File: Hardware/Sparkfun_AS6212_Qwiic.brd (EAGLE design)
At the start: 25.4 x 25.4 mm, 62 parts, among them J1 PTH, J2 QWIIC_RA, J3 QWIIC_RA, U2 AS6212

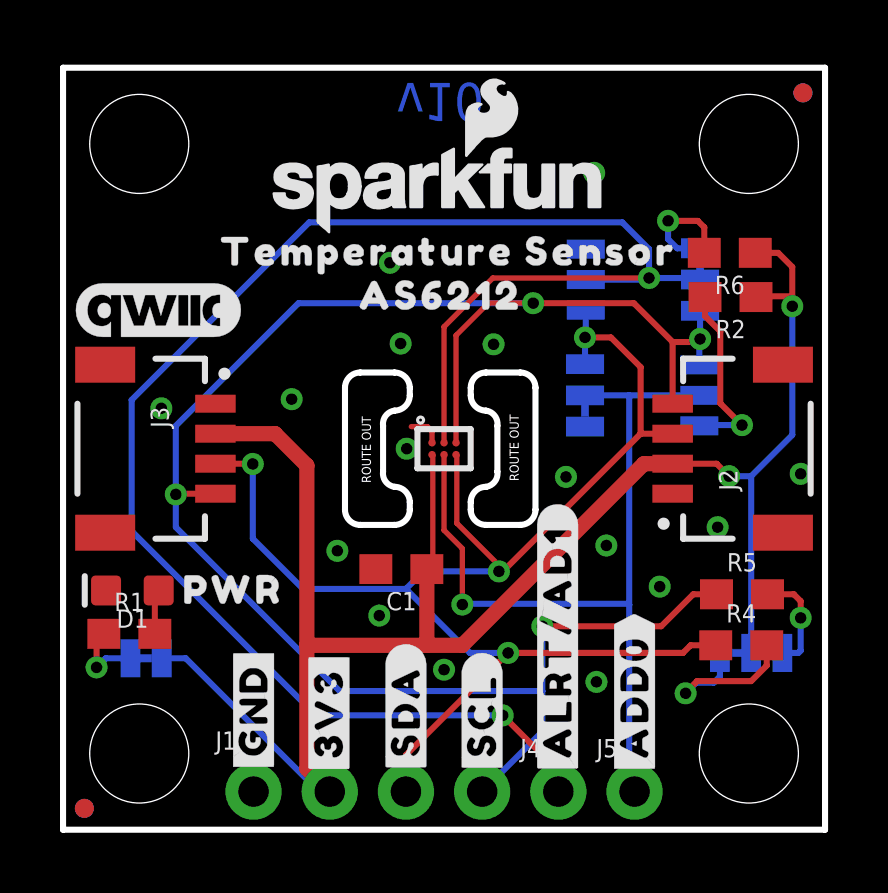
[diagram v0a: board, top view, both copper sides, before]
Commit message: nudged LED and I2C jumpers away from standoffs a tiny bit.
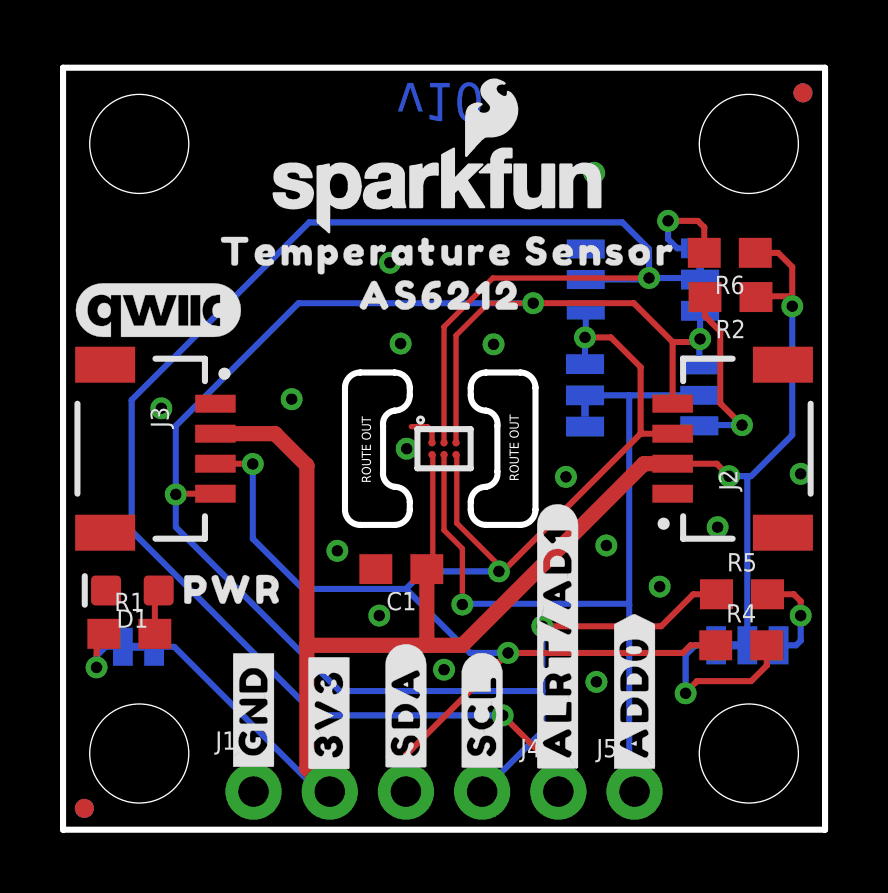
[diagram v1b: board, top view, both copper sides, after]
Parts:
- moved JP1 0.46 mm to (2.51, 6.10)
- moved U$18 0.38 mm to (21.2, 9.70)
- moved U$1 0.36 mm to (2.51, 7.70)
- moved I2C 0.28 mm to (22.8, 6.15)
- moved U$2 0.19 mm to (22.8, 7.75)
- moved U$8 0.13 mm to (21.2, 11.0)
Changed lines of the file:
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@@
 <setting verticaltext="up"/>
 </settings>
-<grid distance="0.05" unitdist="inch" unit="inch" style="lines" multiple="1" display="yes" altdistance="0.005" altunitdist="inch" altunit="inch"/>
+<grid distance="0.05" unitdist="inch" unit="inch" style="lines" multiple="1" display="yes" altdistance="0.001" altunitdist="inch" altunit="inch"/>
 <layers>
 <layer number="1" name="Top" color="4" fill="1" visible="yes" active="yes"/>
@@
 <element name="JP8" library="SparkFun-Hardware" package="STAND-OFF" value="STAND-OFF" x="22.86" y="22.86" smashed="yes"/>
 <element name="JP9" library="SparkFun-Hardware" package="STAND-OFF" value="STAND-OFF" x="2.54" y="22.86" smashed="yes"/>
-<element name="I2C" library="SparkFun-Jumpers" package="SMT-JUMPER_3_2-NC_TRACE_SILK" package3d_urn="urn:adsk.eagle:package:39289/1" value="" x="22.9362" y="5.8928" smashed="yes" rot="MR0">
-<attribute name="NAME" x="22.9362" y="7.0358" size="0.6096" layer="26" font="vector" ratio="20" rot="MR0" align="bottom-center"/>
-<attribute name="VALUE" x="22.9362" y="4.7498" size="0.6096" layer="28" font="vector" ratio="20" rot="MR0" align="top-center"/>
+<element name="I2C" library="SparkFun-Jumpers" package="SMT-JUMPER_3_2-NC_TRACE_SILK" package3d_urn="urn:adsk.eagle:package:39289/1" value="" x="22.8092" y="6.1468" smashed="yes" rot="MR0">
+<attribute name="NAME" x="22.8092" y="7.2898" size="0.6096" layer="26" font="vector" ratio="20" rot="MR0" align="bottom-center"/>
+<attribute name="VALUE" x="22.8092" y="5.0038" size="0.6096" layer="28" font="vector" ratio="20" rot="MR0" align="top-center"/>
 </element>
 <element name="U$15" library="SparkFun-Aesthetics" package="QWIIC_5.5MM" value="" x="3.175" y="17.3228" smashed="yes"/>
@@
 <attribute name="VALUE" x="20.066" y="14.478" size="0.6096" layer="28" font="vector" ratio="20" rot="MR90" align="top-center"/>
 </element>
-<element name="JP1" library="SparkFun-Jumpers" package="SMT-JUMPER_2_NC_TRACE_SILK" package3d_urn="urn:adsk.eagle:package:39281/1" value="LED" x="2.7686" y="5.715" smashed="yes" rot="MR180">
-<attribute name="NAME" x="2.7686" y="4.572" size="0.6096" layer="26" font="vector" ratio="20" rot="MR180" align="bottom-center"/>
-<attribute name="VALUE" x="2.7686" y="6.858" size="0.6096" layer="28" font="vector" ratio="20" rot="MR180" align="top-center"/>
+<element name="JP1" library="SparkFun-Jumpers" package="SMT-JUMPER_2_NC_TRACE_SILK" package3d_urn="urn:adsk.eagle:package:39281/1" value="LED" x="2.5146" y="6.096" smashed="yes" rot="MR180">
+<attribute name="NAME" x="2.5146" y="4.953" size="0.6096" layer="26" font="vector" ratio="20" rot="MR180" align="bottom-center"/>
+<attribute name="VALUE" x="2.5146" y="7.239" size="0.6096" layer="28" font="vector" ratio="20" rot="MR180" align="top-center"/>
 </element>
 <element name="JP2" library="SparkFun-Hardware" package="STAND-OFF" value="STAND-OFF" x="2.54" y="2.54" smashed="yes"/>
@@
 <element name="U$16" library="output" package="SENSOR8" value="" x="4.5466" y="14.1732" smashed="yes" rot="MR0"/>
 <element name="U$17" library="output" package="TEMP9" value="" x="4.6228" y="15.5702" smashed="yes" rot="MR0"/>
-<element name="U$1" library="output" package="#LED#10" value="" x="2.7686" y="7.4422" smashed="yes" rot="MR0"/>
-<element name="U$2" library="output" package="#I2C#11" value="" x="22.86" y="7.5692" smashed="yes" rot="MR0"/>
-<element name="U$8" library="output" package="DEFAULT#11" value="" x="21.1836" y="10.8712" smashed="yes" rot="MR0"/>
-<element name="U$18" library="output" package="0X4812" value="" x="21.2344" y="9.3218" smashed="yes" rot="MR0"/>
+<element name="U$1" library="output" package="#LED#10" value="" x="2.5146" y="7.6962" smashed="yes" rot="MR0"/>
+<element name="U$2" library="output" package="#I2C#11" value="" x="22.7838" y="7.747" smashed="yes" rot="MR0"/>
+<element name="U$8" library="output" package="DEFAULT#11" value="" x="21.1836" y="10.9982" smashed="yes" rot="MR0"/>
+<element name="U$18" library="output" package="0X4812" value="" x="21.2344" y="9.7028" smashed="yes" rot="MR0"/>
 <element name="U$11" library="output" package="#ALRT#AD1#12" value="" x="16.5354" y="6.2738" smashed="yes" rot="MR90"/>
 <element name="U$12" library="output" package="#ALRT#AD1#12" value="" x="16.4846" y="6.2738" smashed="yes" rot="R90"/>
@@
 <wire x1="21.7852" y1="12.2" x2="22.1996" y2="11.7856" width="0.2032" layer="1"/>
 <via x="22.1996" y="11.7856" extent="1-16" drill="0.381"/>
-<wire x1="22.1996" y1="11.7856" x2="22.9362" y2="11.7856" width="0.2032" layer="16"/>
+<wire x1="22.1996" y1="11.7856" x2="22.8092" y2="11.7856" width="0.2032" layer="16"/>
+<wire x1="22.8092" y1="11.7856" x2="22.9362" y2="11.7856" width="0.2032" layer="16"/>
 <wire x1="22.9362" y1="11.7856" x2="24.3078" y2="13.1572" width="0.2032" layer="16"/>
 <wire x1="24.3078" y1="18.757" x2="23.837" y2="19.2278" width="0.2032" layer="1"/>
@@
 <wire x1="24.3078" y1="17.4498" x2="24.3078" y2="17.78" width="0.2032" layer="1"/>
 <wire x1="24.3078" y1="17.78" x2="24.3078" y2="18.757" width="0.2032" layer="1"/>
-<wire x1="22.9362" y1="5.8928" x2="22.9362" y2="11.7856" width="0.2032" layer="16"/>
+<wire x1="22.8092" y1="6.1468" x2="22.8092" y2="11.7856" width="0.2032" layer="16"/>
 <wire x1="8.5344" y1="1.27" x2="8.89" y2="1.27" width="0.2032" layer="16"/>
-<wire x1="8.5344" y1="1.27" x2="4.0894" y2="5.715" width="0.2032" layer="16"/>
+<wire x1="8.5344" y1="1.27" x2="3.7084" y2="6.096" width="0.2032" layer="16"/>
 <wire x1="13.3096" y1="6.1468" x2="12.1158" y2="6.1468" width="0.508" layer="1"/>
 <wire x1="12.1158" y1="6.1468" x2="8.128" y2="6.1468" width="0.508" layer="1"/>
@@
 <via x="24.3078" y="17.4498" extent="1-16" drill="0.381"/>
 <wire x1="24.3078" y1="13.1572" x2="24.3078" y2="17.4498" width="0.2032" layer="16"/>
-<wire x1="4.0894" y1="5.715" x2="3.2893" y2="5.715" width="0.2032" layer="16"/>
+<wire x1="3.7084" y1="6.096" x2="3.0353" y2="6.096" width="0.2032" layer="16"/>
 <wire x1="23.1004" y1="17.7546" x2="23.1258" y2="17.78" width="0.2032" layer="1"/>
 <wire x1="23.1258" y1="17.78" x2="24.3078" y2="17.78" width="0.2032" layer="1"/>
@@
 <contactref element="I2C" pad="1"/>
 <wire x1="23.4814" y1="7.8486" x2="24.3586" y2="7.8486" width="0.2032" layer="1"/>
-<wire x1="24.5872" y1="7.62" x2="24.5872" y2="7.0612" width="0.2032" layer="1"/>
-<via x="24.5872" y="7.0612" extent="1-16" drill="0.381"/>
-<wire x1="24.5872" y1="7.0612" x2="24.5872" y2="5.969" width="0.2032" layer="16"/>
-<wire x1="24.511" y1="5.8928" x2="24.5872" y2="5.969" width="0.2032" layer="16"/>
+<wire x1="24.5872" y1="7.62" x2="24.5872" y2="7.1374" width="0.2032" layer="1"/>
+<via x="24.5872" y="7.1374" extent="1-16" drill="0.381"/>
+<wire x1="24.5872" y1="7.1374" x2="24.5872" y2="6.2992" width="0.2032" layer="16"/>
 <wire x1="24.3586" y1="7.8486" x2="24.5872" y2="7.62" width="0.2032" layer="1"/>
-<wire x1="23.9776" y1="5.8928" x2="24.511" y2="5.8928" width="0.2032" layer="16"/>
+<wire x1="23.8506" y1="6.1468" x2="24.4348" y2="6.1468" width="0.2032" layer="16"/>
+<wire x1="24.4348" y1="6.1468" x2="24.5872" y2="6.2992" width="0.2032" layer="16"/>
 </signal>
 <signal name="N$3">
@@
 <wire x1="20.7518" y1="4.572" x2="20.7518" y2="4.5466" width="0.2032" layer="1"/>
 <via x="20.7518" y="4.5466" extent="1-16" drill="0.381"/>
-<wire x1="20.7518" y1="4.5466" x2="21.1074" y2="4.9022" width="0.2032" layer="16"/>
-<wire x1="21.6916" y1="4.9022" x2="21.1074" y2="4.9022" width="0.2032" layer="16"/>
 <wire x1="23.456" y1="5.4728" x2="22.9362" y2="4.953" width="0.2032" layer="1"/>
-<wire x1="21.8948" y1="5.8928" x2="21.8948" y2="5.1054" width="0.2032" layer="16"/>
-<wire x1="21.8948" y1="5.1054" x2="21.6916" y2="4.9022" width="0.2032" layer="16"/>
+<wire x1="21.7678" y1="6.1468" x2="21.082" y2="6.1468" width="0.2032" layer="16"/>
+<wire x1="21.082" y1="6.1468" x2="20.7518" y2="5.8166" width="0.2032" layer="16"/>
+<wire x1="20.7518" y1="5.8166" x2="20.7518" y2="4.5466" width="0.2032" layer="16"/>
 </signal>
 <signal name="N$7">
@@
 <contactref element="R1" pad="1"/>
 <contactref element="JP1" pad="1"/>
-<wire x1="2.2479" y1="5.715" x2="1.4224" y2="5.715" width="0.2032" layer="16"/>
-<wire x1="1.4224" y1="5.715" x2="1.1176" y2="5.4102" width="0.2032" layer="16"/>
+<wire x1="1.9939" y1="6.096" x2="1.4224" y2="6.096" width="0.2032" layer="16"/>
+<wire x1="1.4224" y1="6.096" x2="1.1176" y2="5.7912" width="0.2032" layer="16"/>
+<wire x1="1.1176" y1="5.7912" x2="1.1176" y2="5.4102" width="0.2032" layer="16"/>
 <via x="1.1176" y="5.4102" extent="1-16" drill="0.381"/>
 <wire x1="1.1176" y1="5.4102" x2="1.1176" y2="6.2856" width="0.2032" layer="1"/>
